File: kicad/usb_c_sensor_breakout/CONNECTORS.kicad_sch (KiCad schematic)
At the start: 1 part

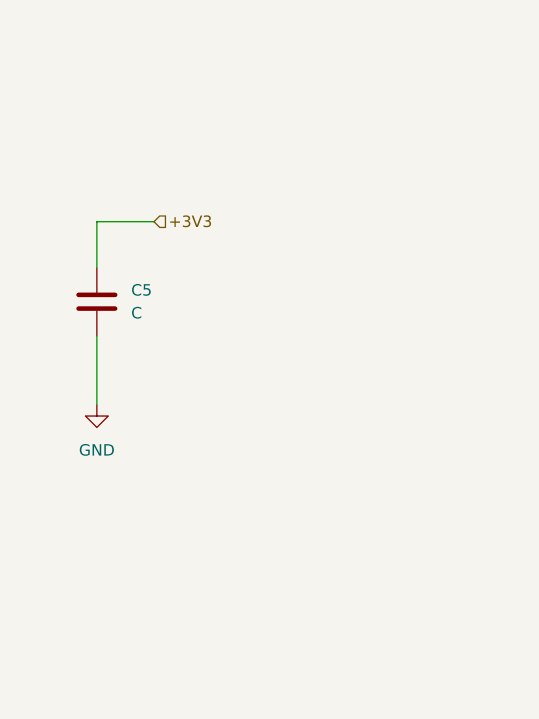
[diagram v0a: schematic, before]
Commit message: Commit3: Regulators + Top-level + I2C sensor upgrade
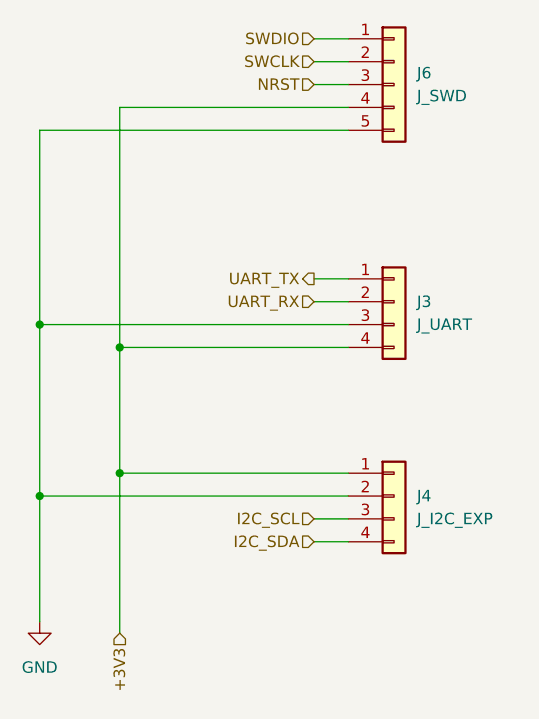
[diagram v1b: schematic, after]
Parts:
- removed C5: C, symbol Device:C
- added J3: J_UART, symbol Connector_Generic:Conn_01x04
- added J4: J_I2C_EXP, symbol Connector_Generic:Conn_01x04
- added J6: J_SWD, symbol Connector_Generic:Conn_01x05
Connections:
- net +3V3: now also J3.4 (Pin_4), J4.1 (Pin_1), J6.4 (Pin_4)
- net GND: now also J3.3 (Pin_3), J4.2 (Pin_2), J6.5 (Pin_5)
- new net I2C_SCL: J4.3 (Pin_3)
- new net I2C_SDA: J4.4 (Pin_4)
- new net NRST: J6.3 (Pin_3)
- new net SWCLK: J6.2 (Pin_2)
- new net SWDIO: J6.1 (Pin_1)
- new net UART_RX: J3.2 (Pin_2)
- new net UART_TX: J3.1 (Pin_1)

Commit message: Commit 4: Updated annotation + footprints
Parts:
- J3, J4: footprint (none) -> Connector_PinHeader_2.54mm:PinHeader_1x04_P2.54mm_Vertical
- J6: footprint (none) -> Connector_PinHeader_2.54mm:PinHeader_1x05_P2.54mm_Vertical
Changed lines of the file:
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@@
 			)
 		)
-		(property "Footprint" ""
+		(property "Footprint" "Connector_PinHeader_2.54mm:PinHeader_1x04_P2.54mm_Vertical"
 			(at 127 81.28 0)
 			(effects
@@
 			)
 		)
-		(property "Footprint" ""
+		(property "Footprint" "Connector_PinHeader_2.54mm:PinHeader_1x04_P2.54mm_Vertical"
 			(at 127 102.87 0)
 			(effects
@@
 			)
 		)
-		(property "Footprint" ""
+		(property "Footprint" "Connector_PinHeader_2.54mm:PinHeader_1x05_P2.54mm_Vertical"
 			(at 127 57.15 0)
 			(effects

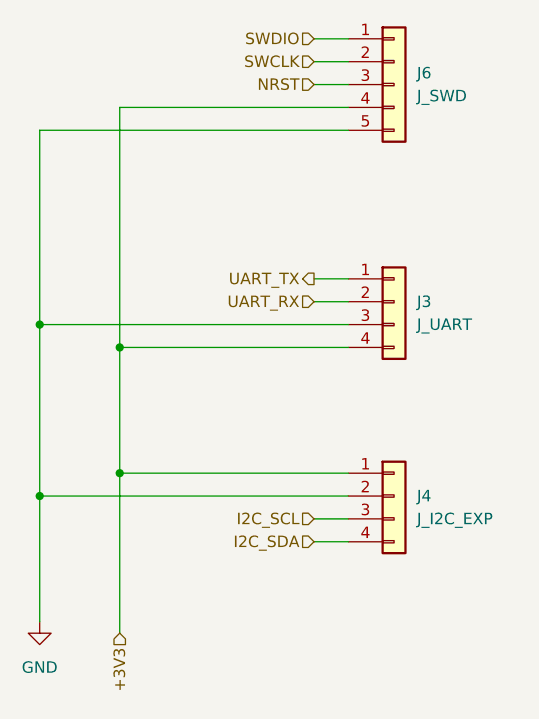
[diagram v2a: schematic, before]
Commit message: Commit 5: MCU + Final Schematic Touches + Labelling + USBc fix
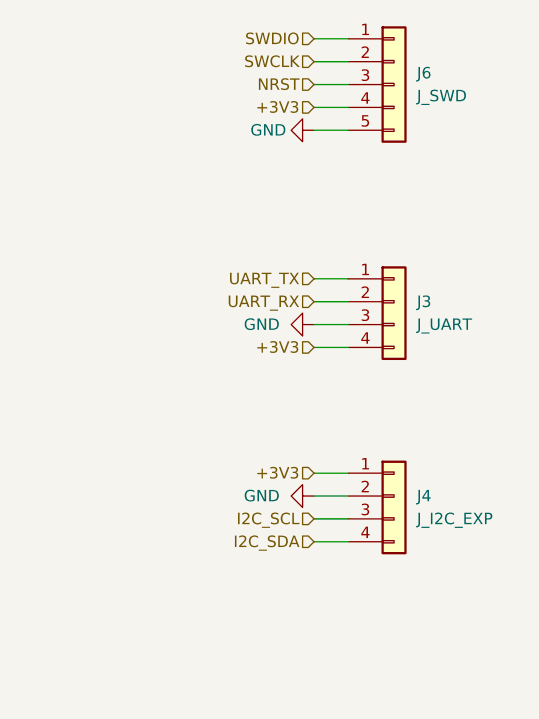
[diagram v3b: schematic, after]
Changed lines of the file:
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@@
 	(generator_version "9.0")
 	(paper "A4")
-	(junction
-		(at 87.63 83.82)
-		(diameter 0)
-		(color 0 0 0 0)
-	)
-	(junction
-		(at 96.52 100.33)
-		(diameter 0)
-		(color 0 0 0 0)
-	)
-	(junction
-		(at 96.52 86.36)
-		(diameter 0)
-		(color 0 0 0 0)
-	)
-	(junction
-		(at 87.63 102.87)
-		(diameter 0)
-		(color 0 0 0 0)
-	)
-	(wire
-		(pts
-			(xy 121.92 59.69) (xy 96.52 59.69)
-		)
-		(stroke
-			(width 0)
-			(type default)
-		)
-	)
-	(wire
-		(pts
-			(xy 87.63 83.82) (xy 87.63 62.23)
-		)
-		(stroke
-			(width 0)
-			(type default)
-		)
-	)
-	(wire
-		(pts
-			(xy 87.63 102.87) (xy 121.92 102.87)
+	(wire
+		(pts
+			(xy 118.11 83.82) (xy 121.92 83.82)
 		)
 		(stroke
@@
 	(wire
 		(pts
-			(xy 87.63 62.23) (xy 121.92 62.23)
-		)
-		(stroke
-			(width 0)
-			(type default)
-		)
-	)
-	(wire
-		(pts
 			(xy 118.11 52.07) (xy 121.92 52.07)
 		)
@@
 	(wire
 		(pts
-			(xy 87.63 102.87) (xy 87.63 83.82)
+			(xy 118.11 62.23) (xy 121.92 62.23)
+		)
+		(stroke
+			(width 0)
+			(type default)
+		)
+	)
+	(wire
+		(pts
+			(xy 118.11 100.33) (xy 121.92 100.33)
+		)
+		(stroke
+			(width 0)
+			(type default)
+		)
+	)
+	(wire
+		(pts
+			(xy 118.11 59.69) (xy 121.92 59.69)
+		)
+		(stroke
+			(width 0)
+			(type default)
+		)
+	)
+	(wire
+		(pts
+			(xy 118.11 86.36) (xy 121.92 86.36)
 		)
 		(stroke
@@
 	(wire
 		(pts
-			(xy 96.52 100.33) (xy 121.92 100.33)
-		)
-		(stroke
-			(width 0)
-			(type default)
-		)
-	)
-	(wire
-		(pts
-			(xy 87.63 116.84) (xy 87.63 102.87)
+			(xy 118.11 102.87) (xy 121.92 102.87)
 		)
 		(stroke
@@
 	(wire
 		(pts
-			(xy 96.52 86.36) (xy 121.92 86.36)
-		)
-		(stroke
-			(width 0)
-			(type default)
-		)
-	)
-	(wire
-		(pts
 			(xy 118.11 81.28) (xy 121.92 81.28)
 		)
@@
 	(wire
 		(pts
-			(xy 87.63 83.82) (xy 121.92 83.82)
-		)
-		(stroke
-			(width 0)
-			(type default)
-		)
-	)
-	(wire
-		(pts
-			(xy 96.52 118.11) (xy 96.52 100.33)
-		)
-		(stroke
-			(width 0)
-			(type default)
-		)
-	)
-	(wire
-		(pts
-			(xy 96.52 100.33) (xy 96.52 86.36)
-		)
-		(stroke
-			(width 0)
-			(type default)
-		)
-	)
-	(wire
-		(pts
 			(xy 118.11 105.41) (xy 121.92 105.41)
 		)
@@
 		)
 	)
-	(wire
-		(pts
-			(xy 96.52 59.69) (xy 96.52 86.36)
-		)
-		(stroke
-			(width 0)
-			(type default)
-		)
-	)
 	(hierarchical_label "SWDIO"
 		(shape input)
@@
 	)
 	(hierarchical_label "UART_TX"
-		(shape output)
+		(shape input)
 		(at 118.11 78.74 180)
 		(effects
@@
 	(hierarchical_label "+3V3"
 		(shape input)
-		(at 96.52 118.11 270)
+		(at 118.11 86.36 180)
 		(effects
 			(font
@@
 		)
 	)
+	(hierarchical_label "+3V3"
+		(shape input)
+		(at 118.11 59.69 180)
+		(effects
+			(font
+				(size 1.27 1.27)
+			)
+			(justify right)
+		)
+	)
 	(hierarchical_label "I2C_SCL"
 		(shape input)
@@
 		(shape input)
 		(at 118.11 81.28 180)
+		(effects
+			(font
+				(size 1.27 1.27)
+			)
+			(justify right)
+		)
+	)
+	(hierarchical_label "+3V3"
+		(shape input)
+		(at 118.11 100.33 180)
 		(effects
 			(font
@@
 	(symbol
 		(lib_id "power:GND")
-		(at 87.63 116.84 0)
+		(at 118.11 62.23 270)
 		(unit 1)
 		(exclude_from_sim no)
@@
 		(on_board yes)
 		(dnp no)
-		(fields_autoplaced yes)
 		(property "Reference" "#PWR04"
-			(at 87.63 123.19 0)
+			(at 111.76 62.23 0)
 			(effects
 				(font
@@
 		)
 		(property "Value" "GND"
-			(at 87.63 121.92 0)
+			(at 113.03 62.23 90)
 			(effects
 				(font
@@
 		)
 		(property "Footprint" ""
-			(at 87.63 116.84 0)
+			(at 118.11 62.23 0)
 			(effects
 				(font
@@
 		)
 		(property "Datasheet" ""
-			(at 87.63 116.84 0)
+			(at 118.11 62.23 0)
 			(effects
 				(font
@@
 		)
 		(property "Description" "Power symbol creates a global label with name \"GND\" , ground"
-			(at 87.63 116.84 0)
+			(at 118.11 62.23 0)
 			(effects
 				(font
@@
 		)
 		(instances
-			(project ""
+			(project "usb_c_sensor_breakout"
 				(path "/a2072585-dfc7-469c-b616-14a83342abb9/6f181b3f-6072-4b32-b04c-1561f838d1fb"
 					(reference "#PWR04")
@@
 					(unit 1)
 				)
+			)
+		)
+	)
+	(symbol
+		(lib_id "power:GND")
+		(at 118.11 83.82 270)
+		(unit 1)
+		(exclude_from_sim no)
+		(in_bom yes)
+		(on_board yes)
+		(dnp no)
+		(fields_autoplaced yes)
+		(property "Reference" "#PWR08"
+			(at 111.76 83.82 0)
+			(effects
+				(font
+					(size 1.27 1.27)
+				)
+				(hide yes)
+			)
+		)
+		(property "Value" "GND"
+			(at 114.3 83.8199 90)
+			(effects
+				(font
+					(size 1.27 1.27)
+				)
+				(justify right)
+			)
+		)
+		(property "Footprint" ""
+			(at 118.11 83.82 0)
+			(effects
+				(font
+					(size 1.27 1.27)
+				)
+				(hide yes)
+			)
+		)
+		(property "Datasheet" ""
+			(at 118.11 83.82 0)
+			(effects
+				(font
+					(size 1.27 1.27)
+				)
+				(hide yes)
+			)
+		)
+		(property "Description" "Power symbol creates a global label with name \"GND\" , ground"
+			(at 118.11 83.82 0)
+			(effects
+				(font
+					(size 1.27 1.27)
+				)
+				(hide yes)
+			)
+		)
+		(pin "1"
+		)
+		(instances
+			(project "usb_c_sensor_breakout"
+				(path "/a2072585-dfc7-469c-b616-14a83342abb9/6f181b3f-6072-4b32-b04c-1561f838d1fb"
+					(reference "#PWR08")
+					(unit 1)
+				)
+			)
+		)
+	)
+	(symbol
+		(lib_id "power:GND")
+		(at 118.11 102.87 270)
+		(unit 1)
+		(exclude_from_sim no)
+		(in_bom yes)
+		(on_board yes)
+		(dnp no)
+		(fields_autoplaced yes)
+		(property "Reference" "#PWR09"
+			(at 111.76 102.87 0)
+			(effects
+				(font
+					(size 1.27 1.27)
+				)
+				(hide yes)
+			)
+		)
+		(property "Value" "GND"
+			(at 114.3 102.8699 90)
+			(effects
+				(font
+					(size 1.27 1.27)
+				)
+				(justify right)
+			)
+		)
+		(property "Footprint" ""
+			(at 118.11 102.87 0)
+			(effects
+				(font
+					(size 1.27 1.27)
+				)
+				(hide yes)
+			)
+		)
+		(property "Datasheet" ""
+			(at 118.11 102.87 0)
+			(effects
+				(font
+					(size 1.27 1.27)
+				)
+				(hide yes)
+			)
+		)
+		(property "Description" "Power symbol creates a global label with name \"GND\" , ground"
+			(at 118.11 102.87 0)
+			(effects
+				(font
+					(size 1.27 1.27)
+				)
+				(hide yes)
+			)
+		)
+		(pin "1"
+		)
+		(instances
+			(project "usb_c_sensor_breakout"
+				(path "/a2072585-dfc7-469c-b616-14a83342abb9/6f181b3f-6072-4b32-b04c-1561f838d1fb"
+					(reference "#PWR09")
+					(unit 1)
+				)

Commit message: Commit 6: Finished PCB + Updated Schematic
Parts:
- renumbered J6 to J5
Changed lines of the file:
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@@
 	)
 	(hierarchical_label "SWDIO"
-		(shape input)
+		(shape bidirectional)
 		(at 118.11 52.07 180)
 		(effects
@@
 	)
 	(hierarchical_label "UART_TX"
-		(shape input)
+		(shape output)
 		(at 118.11 78.74 180)
 		(effects
@@
 	)
 	(hierarchical_label "I2C_SDA"
-		(shape input)
+		(shape bidirectional)
 		(at 118.11 107.95 180)
 		(effects
@@
 	)
 	(hierarchical_label "I2C_SCL"
-		(shape input)
+		(shape bidirectional)
 		(at 118.11 105.41 180)
 		(effects
@@
 	)
 	(hierarchical_label "NRST"
-		(shape input)
+		(shape bidirectional)
 		(at 118.11 57.15 180)
 		(effects
@@
 		(dnp no)
 		(fields_autoplaced yes)
-		(property "Reference" "J6"
+		(property "Reference" "J5"
 			(at 129.54 55.8799 0)
 			(effects
@@
 			(project ""
 				(path "/a2072585-dfc7-469c-b616-14a83342abb9/6f181b3f-6072-4b32-b04c-1561f838d1fb"
-					(reference "J6")
+					(reference "J5")
 					(unit 1)
 				)
